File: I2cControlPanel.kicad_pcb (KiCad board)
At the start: 2 copper layers, 100 x 100 mm, 52 parts, among them J1 JoystickL, J2 Conn_01x06, J3 Conn_01x04, J4 Conn_01x04, J5 JoystickR, J6 Conn_01x04, SW6 SW_Push, U1 NJM12888F33, U2 ATmega328PB-MU, U3 AQM0802

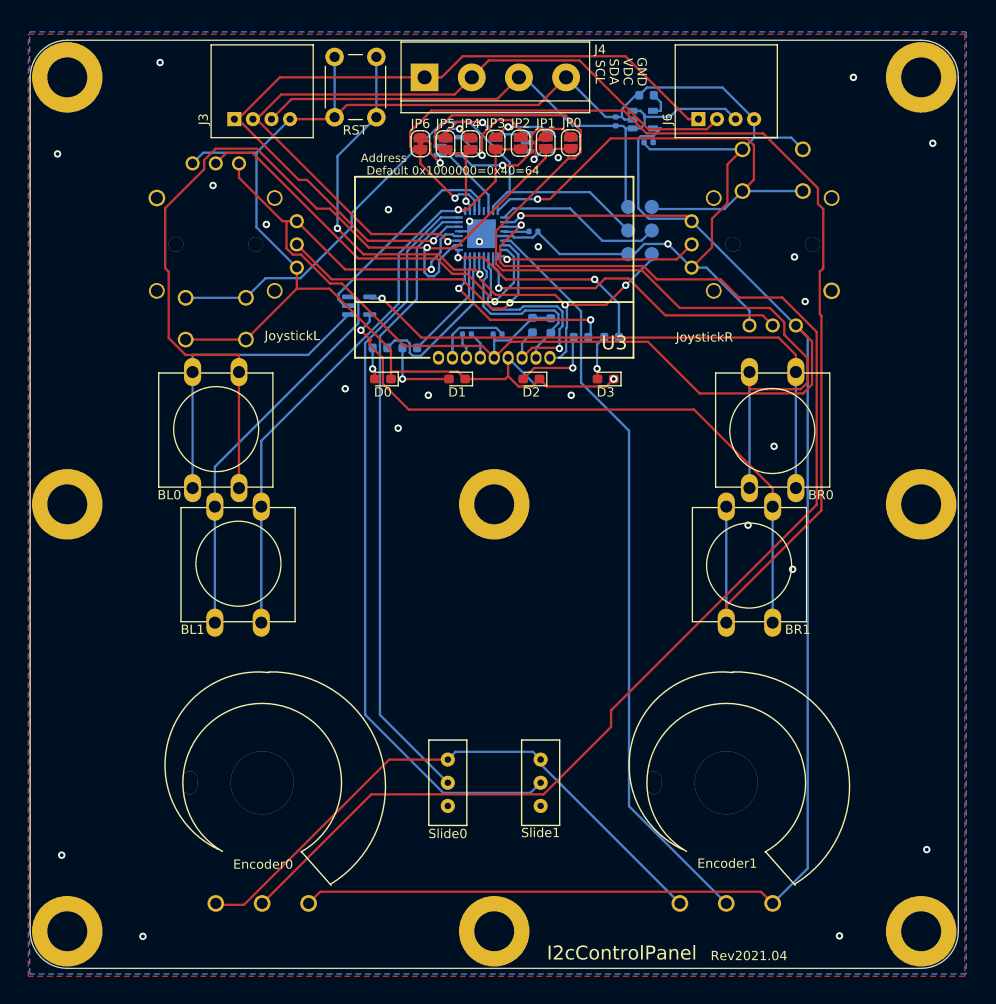
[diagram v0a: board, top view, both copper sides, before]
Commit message: Change rotery encoder and remove pull up for internal i2c
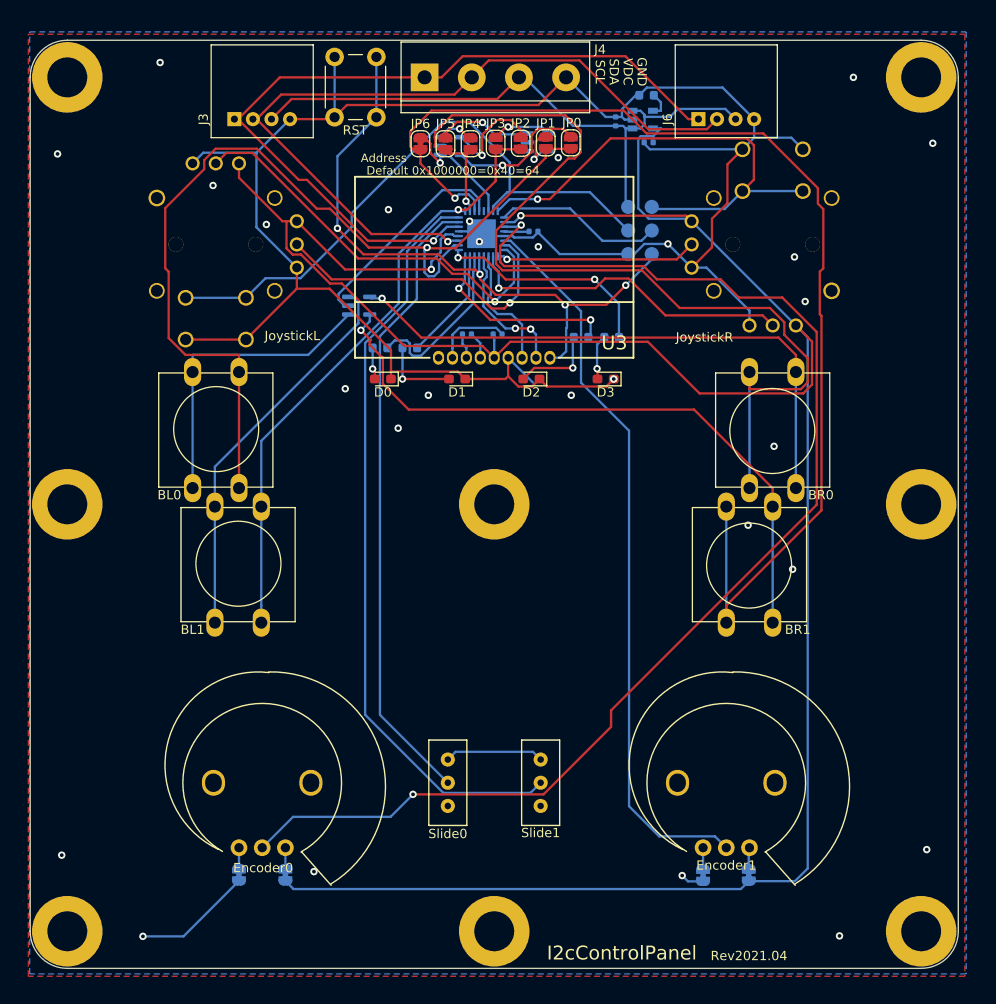
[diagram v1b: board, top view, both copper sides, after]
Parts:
- removed R5, R6: 10k, Resistor_SMD:R_0603_1608Metric
- added JP10: NC, Jumper:SolderJumper-2_P1.3mm_Bridged_RoundedPad1.0x1.5mm, B.Cu at (127.4, 139.9)
- added JP7: NC, Jumper:SolderJumper-2_P1.3mm_Bridged_RoundedPad1.0x1.5mm, B.Cu at (72.5, 139.9)
- added JP8: NC, Jumper:SolderJumper-2_P1.3mm_Bridged_RoundedPad1.0x1.5mm, B.Cu at (122.5, 140.0)
- added JP9: NC, Jumper:SolderJumper-2_P1.3mm_Bridged_RoundedPad1.0x1.5mm, B.Cu at (77.5, 139.9)
- Encoder0, Encoder1: footprint my-kicad-footprints:Volume -> my-kicad-footprints:RoteryEncoderWithPowerLabel
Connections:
- Encoder0 pad 1: +3V3 -> Net-(Encoder0-Pad1)
- Encoder0 pad 3: GND -> Net-(Encoder0-Pad3)
- Encoder1 pad 1: +3V3 -> Net-(Encoder1-Pad1)
- Encoder1 pad 3: GND -> Net-(Encoder1-Pad3)
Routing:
- net GND: track 292.8 -> 255.4 mm, vias 25 -> 27
- net /SDA_inside: track 25.9 -> 13.6 mm, vias 1 -> 0
- net +3V3: track 287.2 -> 281.3 mm
- net /SCL_inside: track 20.1 -> 15.1 mm, vias 0 -> 2
- net /Rotery1: track 141.3 -> 138.8 mm, vias 1 -> 2
- net /Rotery2: track 81.7 -> 79.2 mm
- net Net-(Encoder1-Pad3): track 0.00 -> 2.33 mm
- net Net-(Encoder1-Pad1): track 0.00 -> 2.32 mm
- net Net-(Encoder0-Pad3): track 0.00 -> 2.28 mm
- net Net-(Encoder0-Pad1): track 0.00 -> 2.28 mm

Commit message: Update revision to 2021.05
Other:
- board text added: "Rev2021.05"
- board text removed: "Rev2021.04"
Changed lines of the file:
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@@
   (gr_arc (start 54 146) (end 54 150) (angle 90) (layer Edge.Cuts) (width 0.05))
   (gr_arc (start 54 54) (end 50 54) (angle 90) (layer Edge.Cuts) (width 0.05))
-  (gr_text Rev2021.04 (at 127.45 148.65) (layer F.SilkS)
+  (gr_text Rev2021.05 (at 127.45 148.65) (layer F.SilkS)
     (effects (font (size 1 1) (thickness 0.15)))
   )

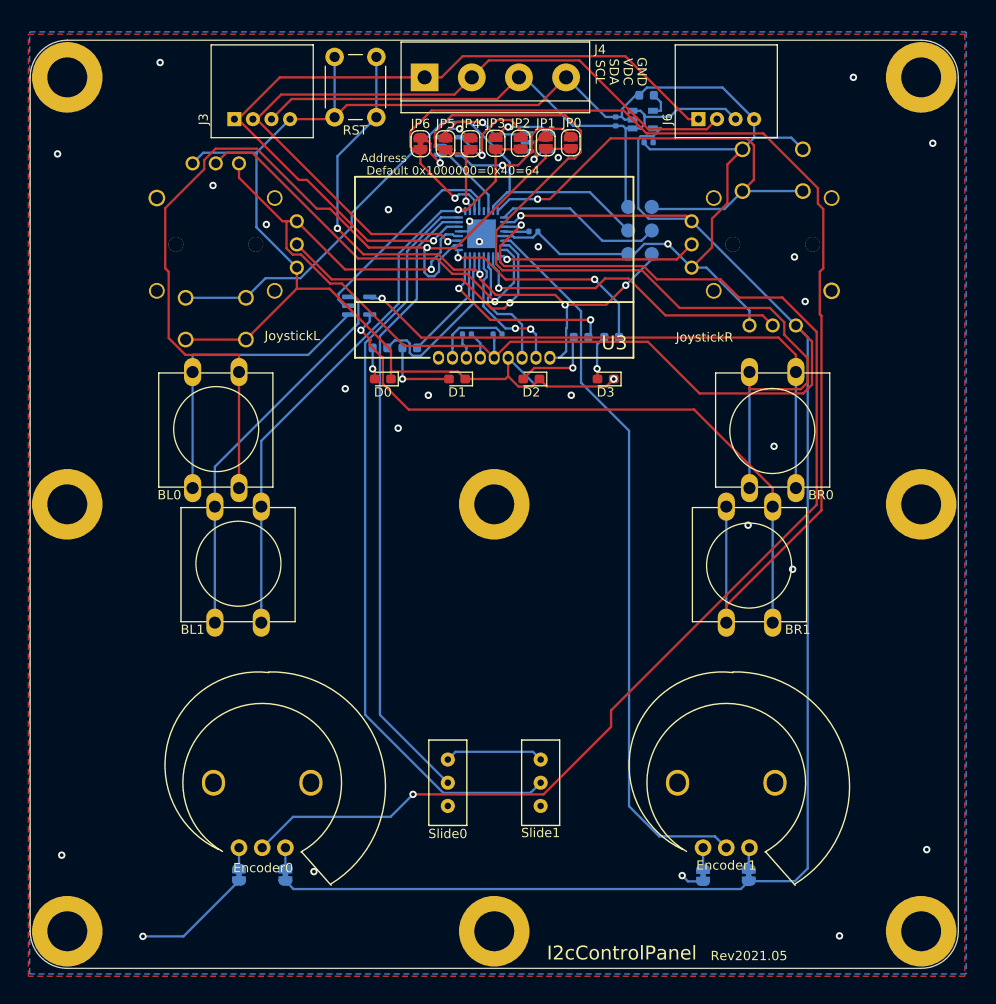
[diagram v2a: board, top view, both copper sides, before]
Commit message: Update for KiCad6
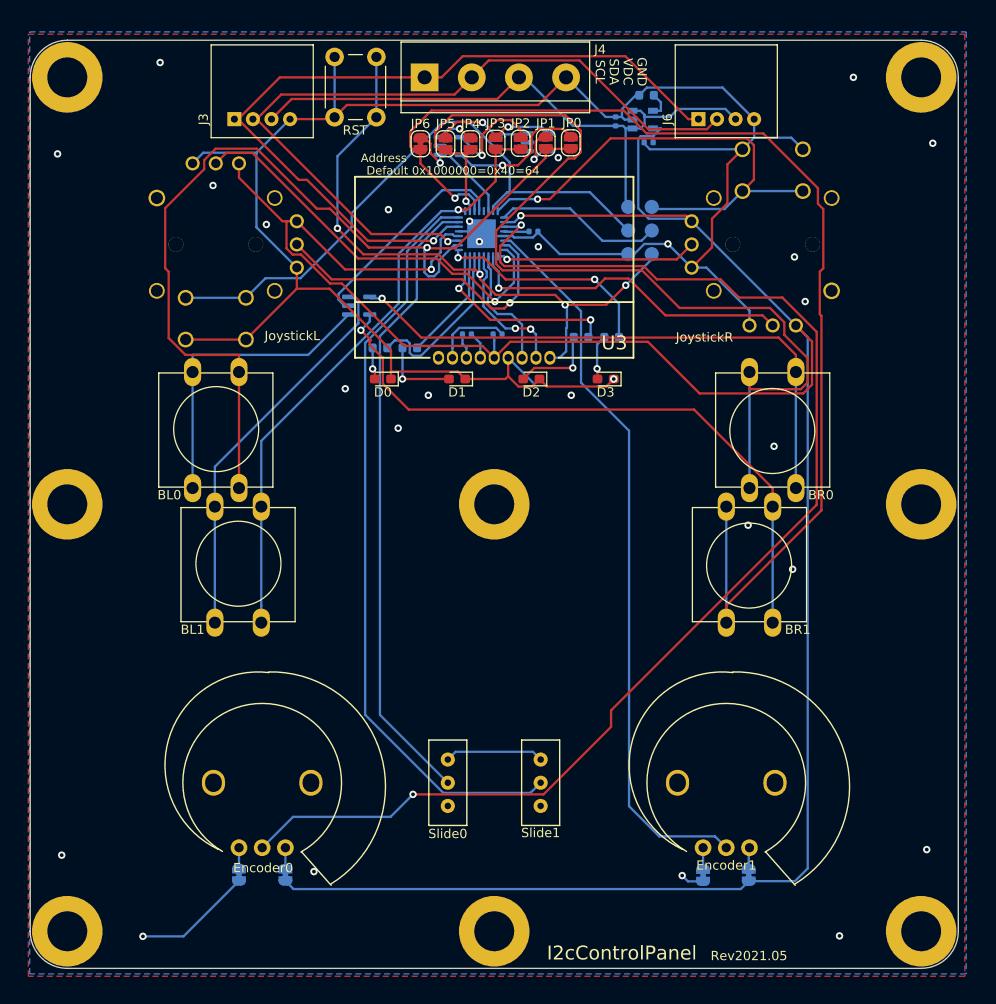
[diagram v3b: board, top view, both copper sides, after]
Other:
- net class Default removed

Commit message: Assign asukiaaa-kicad- symbols and footprints
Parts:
- D4, D5, D6: footprint my-kicad-footprints:SC-74-5_1.6x2.9mm_P0.95mm -> asukiaaa-kicad-footprints:SC-74-5_1.6x2.9mm_P0.95mm
- Encoder0, Encoder1: footprint my-kicad-footprints:RoteryEncoderWithPowerLabel -> asukiaaa-kicad-footprints:RoteryEncoderWithPowerLabel
- J1, J5: footprint my-kicad-footprints:PS4tJoystick -> asukiaaa-kicad-footprints:PS4tJoystick
- J2: footprint my-kicad-footprints:2x03_P2.54mm_Pads -> asukiaaa-kicad-footprints:2x03_P2.54mm_Pads
- Slide0, Slide1: footprint my-kicad-footprints:SlideSwitch_SS12D01G4_2posi_1line -> asukiaaa-kicad-footprints:SlideSwitch_SS12D01G4_2posi_1line
- U3: footprint my-kicad-footprints:AQM0802A-RN-GBW -> asukiaaa-kicad-footprints:AQM0802A-RN-GBW
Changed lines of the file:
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@@
     )
   )
-  (footprint "my-kicad-footprints:AQM0802A-RN-GBW" (layer "F.Cu")
+  (footprint "asukiaaa-kicad-footprints:AQM0802A-RN-GBW" (layer "F.Cu")
     (at 100 74.462)
     (descr "http://akizukidenshi.com/download/ds/xiamen/AQM0802.pdf")
@@
       ))
   )
-  (footprint "my-kicad-footprints:PS4tJoystick" (layer "F.Cu")
+  (footprint "asukiaaa-kicad-footprints:PS4tJoystick" (layer "F.Cu")
     (at 70 72 90)
     (attr through_hole)
@@
     (pad "NC" thru_hole circle locked (at 0 4.3 90) (size 1.6 1.6) (drill 1.6) (layers *.Cu *.Mask))
   )
-  (footprint "my-kicad-footprints:PS4tJoystick" (layer "F.Cu")
+  (footprint "asukiaaa-kicad-footprints:PS4tJoystick" (layer "F.Cu")
     (at 130 72 -90)
     (attr through_hole)
@@
     (pad "NC" thru_hole circle locked (at -5 6.35 270) (size 1.7 1.7) (drill 1.3) (layers *.Cu *.Mask))
   )
-  (footprint "my-kicad-footprints:RoteryEncoderWithPowerLabel" (layer "F.Cu")
+  (footprint "asukiaaa-kicad-footprints:RoteryEncoderWithPowerLabel" (layer "F.Cu")
     (at 75 130)
     (descr "http://akizukidenshi.com/catalog/g/gP-00244/")
@@
     (pad "NC" thru_hole oval locked (at -5.25 0) (size 2.5 2.8) (drill oval 1.8 2) (layers *.Cu *.Mask))
   )
-  (footprint "my-kicad-footprints:RoteryEncoderWithPowerLabel" (layer "F.Cu")
+  (footprint "asukiaaa-kicad-footprints:RoteryEncoderWithPowerLabel" (layer "F.Cu")
     (at 125 130)
     (descr "http://akizukidenshi.com/catalog/g/gP-00244/")
@@
     (pad "NC" thru_hole oval locked (at -5.25 0) (size 2.5 2.8) (drill oval 1.8 2) (layers *.Cu *.Mask))
   )
-  (footprint "my-kicad-footprints:SlideSwitch_SS12D01G4_2posi_1line" (layer "F.Cu")
+  (footprint "asukiaaa-kicad-footprints:SlideSwitch_SS12D01G4_2posi_1line" (layer "F.Cu")
     (at 95 130 -90)
     (descr "https://akizukidenshi.com/download/ds/switronic/SS12D01G4-G_2.pdf")
@@
     )
   )
-  (footprint "my-kicad-footprints:SlideSwitch_SS12D01G4_2posi_1line" (layer "F.Cu")
+  (footprint "asukiaaa-kicad-footprints:SlideSwitch_SS12D01G4_2posi_1line" (layer "F.Cu")
     (at 105 130 -90)
     (descr "https://akizukidenshi.com/download/ds/switronic/SS12D01G4-G_2.pdf")
@@
     )
   )
-  (footprint "my-kicad-footprints:2x03_P2.54mm_Pads" (layer "B.Cu")
+  (footprint "asukiaaa-kicad-footprints:2x03_P2.54mm_Pads" (layer "B.Cu")
     (at 115.7 70.5 180)
     (descr "surface-mounted straight pin header, 2x03, 2.54mm pitch, double rows")
@@
     )
   )
-  (footprint "my-kicad-footprints:SC-74-5_1.6x2.9mm_P0.95mm" (layer "B.Cu")
+  (footprint "asukiaaa-kicad-footprints:SC-74-5_1.6x2.9mm_P0.95mm" (layer "B.Cu")
     (at 95.3125 61.4)
     (descr "SC-74, 5 Pin")
@@
     )
   )
-  (footprint "my-kicad-footprints:SC-74-5_1.6x2.9mm_P0.95mm" (layer "B.Cu")
+  (footprint "asukiaaa-kicad-footprints:SC-74-5_1.6x2.9mm_P0.95mm" (layer "B.Cu")
     (at 104.7 61)
     (descr "SC-74, 5 Pin")
@@
     )
   )
-  (footprint "my-kicad-footprints:SC-74-5_1.6x2.9mm_P0.95mm" (layer "B.Cu")
+  (footprint "asukiaaa-kicad-footprints:SC-74-5_1.6x2.9mm_P0.95mm" (layer "B.Cu")
     (at 85.45 78.6)
     (descr "SC-74, 5 Pin")

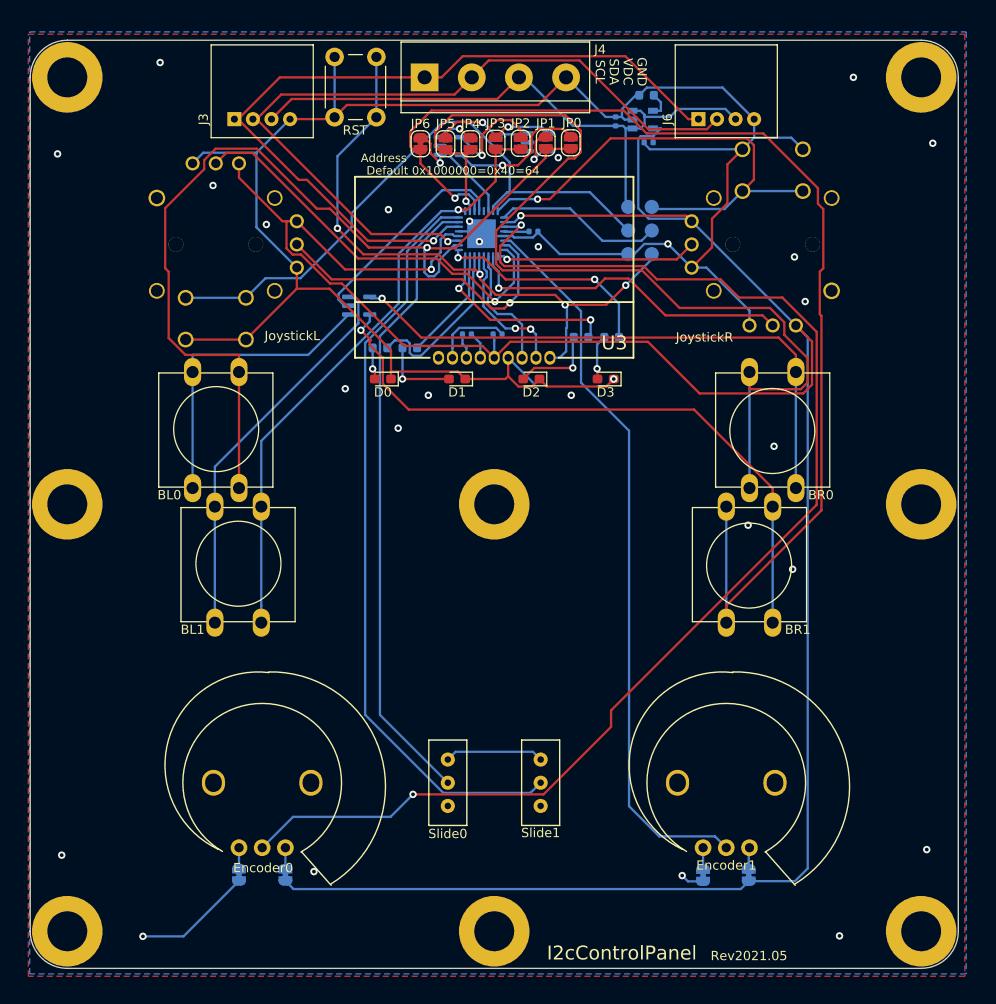
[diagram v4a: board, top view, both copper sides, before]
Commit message: Change mounting hole as bare
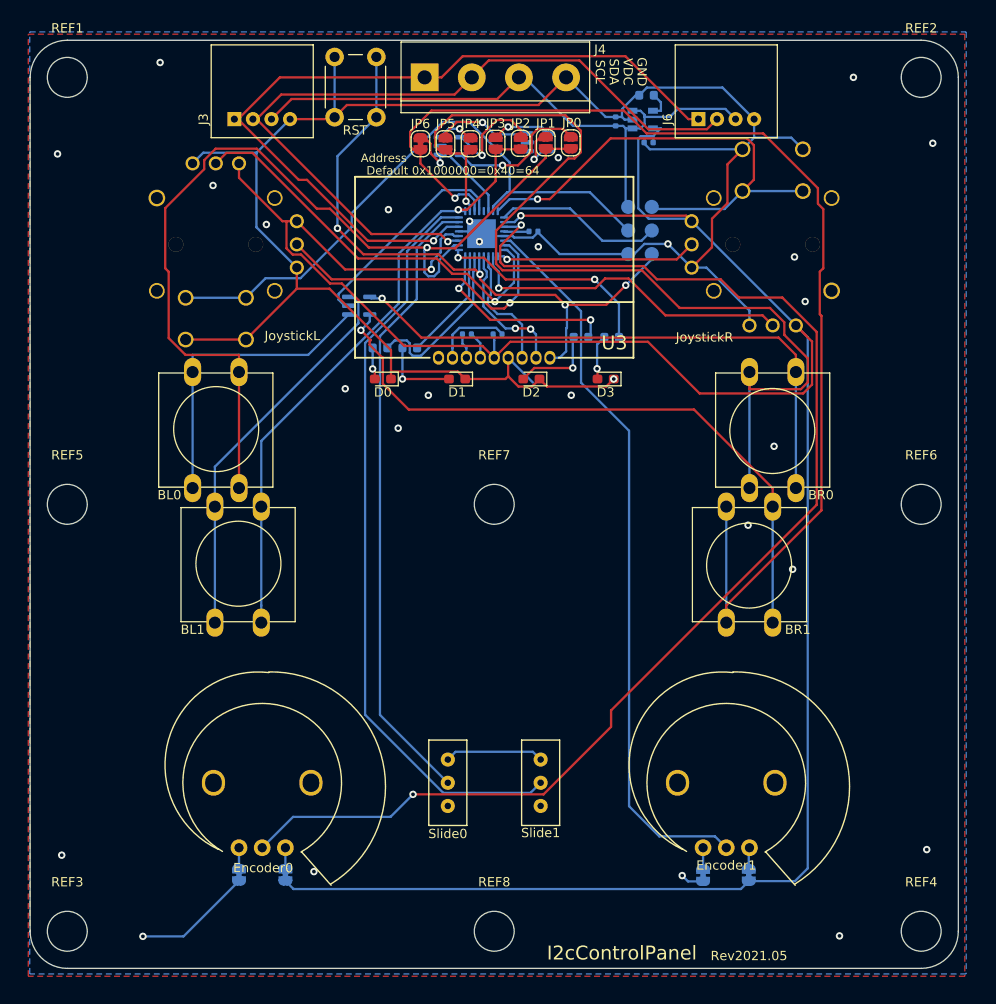
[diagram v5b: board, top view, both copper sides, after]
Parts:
- REF1, REF2, REF3, REF4, REF5, REF6, REF7, REF8: value MountingHole_4.3mm_M4_ISO7380_Pad -> MountingHole_4.3mm_M4_bare; footprint MountingHole:MountingHole_4.3mm_M4_ISO7380_Pad -> asukiaaa-kicad-footprints:MountingHole_4.3mm_M4_bare

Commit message: Update revision as 2022.07
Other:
- board text added: "Rev2022.07"
- board text removed: "Rev2021.05"
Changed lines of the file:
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@@
     (effects (font (size 1 1) (thickness 0.15)))
   )
-  (gr_text "Rev2021.05" (at 127.45 148.65) (layer "F.SilkS")
+  (gr_text "Rev2022.07" (at 127.45 148.65) (layer "F.SilkS")
     (effects (font (size 1 1) (thickness 0.15)))
   )

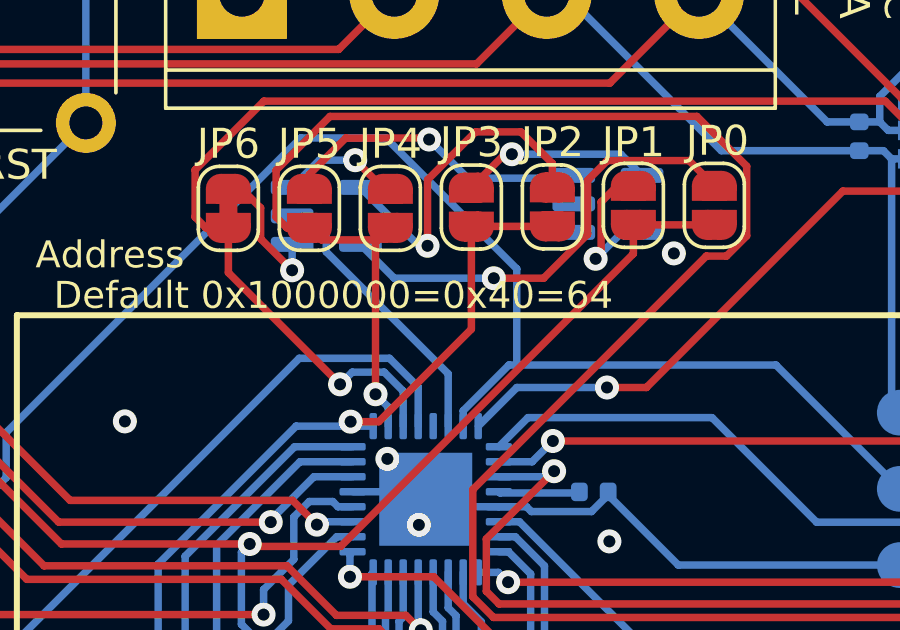
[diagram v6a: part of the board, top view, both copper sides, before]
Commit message: Joint missing BtnSig1 line on pcb
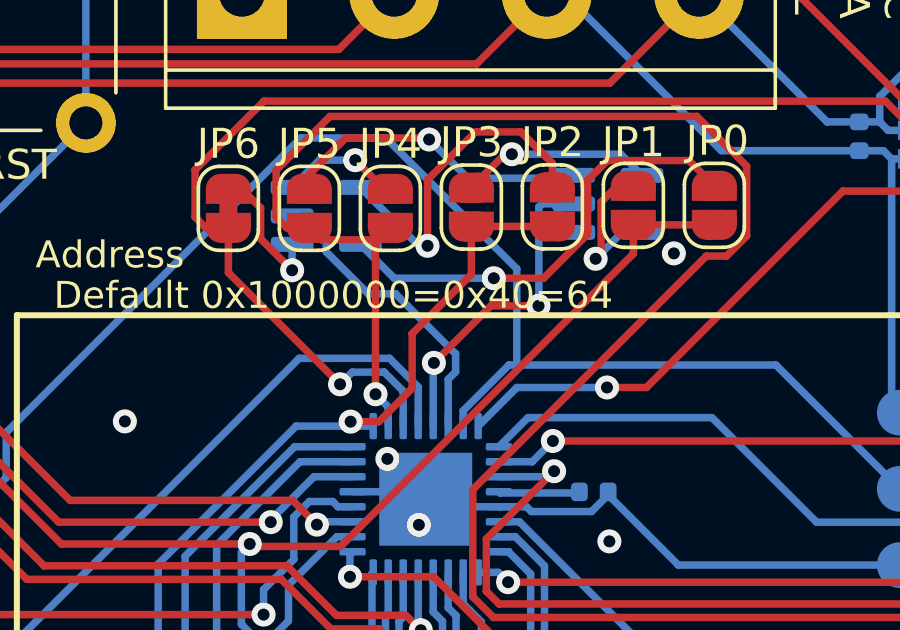
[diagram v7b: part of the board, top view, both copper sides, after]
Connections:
- D5 pad 1: Net-(D5-Pad1) -> unconnected-(D5-Pad1)
- D5 pad 2: Net-(D5-Pad2) -> /BtnSig1
- Slide0 pad 3: Net-(Slide0-Pad3) -> unconnected-(Slide0-Pad3)
- Slide1 pad 3: Net-(Slide1-Pad3) -> unconnected-(Slide1-Pad3)
- U3 pad 1: Net-(U3-Pad1) -> unconnected-(U3-Pad1)
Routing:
- net /BtnSig1: track 0.00 -> 10.9 mm, vias 0 -> 2
- net /BtnSig2: track 9.41 -> 10.1 mm
